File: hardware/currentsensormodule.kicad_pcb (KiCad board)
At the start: 2 copper layers, 92 x 54.5 mm, 110 parts, among them J101 USART, J102 STLink, J103 Sensor1, J104 Sensor2, J105 RJ45, J106 RJ45, U101 LM324, U103 K78L15-1000R3, U104 K78L15-1000R3, U105 AMS1117-5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

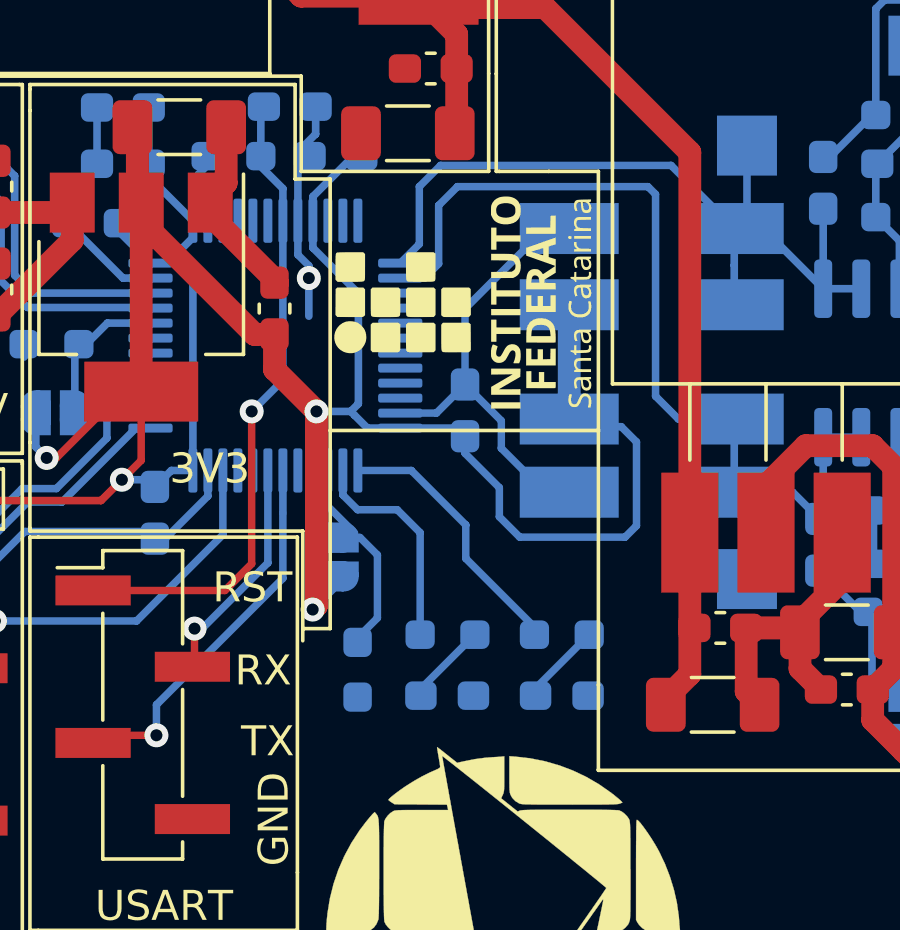
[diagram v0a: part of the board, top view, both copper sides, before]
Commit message: Pequenas mudanças na silkscreen
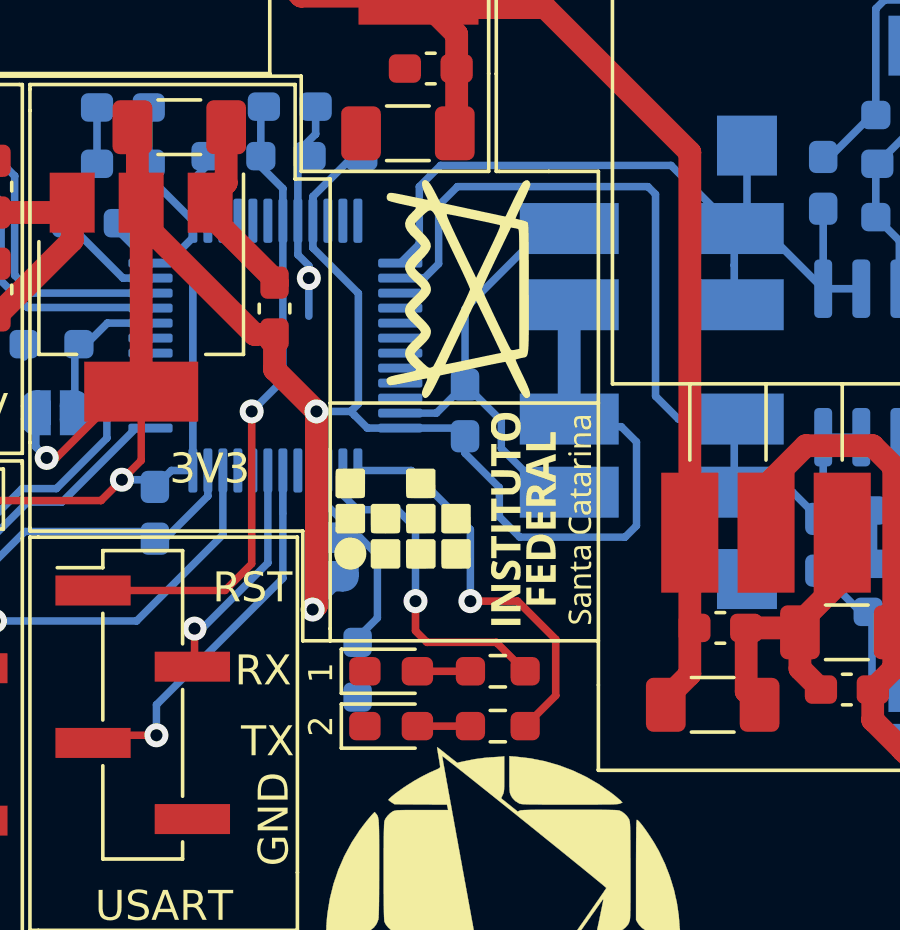
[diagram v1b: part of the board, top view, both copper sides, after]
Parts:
- added SYM105: SYM_Radioactive_Radiation_Small, naolavar:naolavar, F.Cu at (135.8, 98.1)
- D105, D106, R120, R121: moved to F.Cu
- moved SYM102 7.21 mm to (135.9, 105.8)
- moved D106 5.78 mm to (133.6, 112.7), turned to 0 degrees
- moved R120 3.72 mm to (137.1, 112.7), turned to 180 degrees
- moved R121 2.07 mm to (137.1, 110.9), turned to 180 degrees
- moved D105 2.04 mm to (133.6, 110.9), turned to 0 degrees
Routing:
- net /STM32/LED0: track 8.70 -> 13.6 mm, vias 0 -> 1
- net /STM32/LED1: track 7.31 -> 11.3 mm, vias 0 -> 1
- net Net-(D105-Pad2): track 2.78 -> 1.77 mm
- net Net-(D106-Pad2): track 2.77 -> 1.77 mm
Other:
- board text added: "1"
- board text added: "2"
- board text removed: "LED0"
- board text removed: "LED1"

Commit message: hardware: Design constraints adjusted according to JLC pcb limits
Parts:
- moved LOGO101 18.9 mm to (161.2, 76.8)
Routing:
- net +3V3: track 97.9 -> 97.2 mm
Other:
- board text added: "Designed by Zenite Solar Boat Team - github.com/ZeniteSolar"
- board text added: "github.com/ZeniteSolar/MSC22"

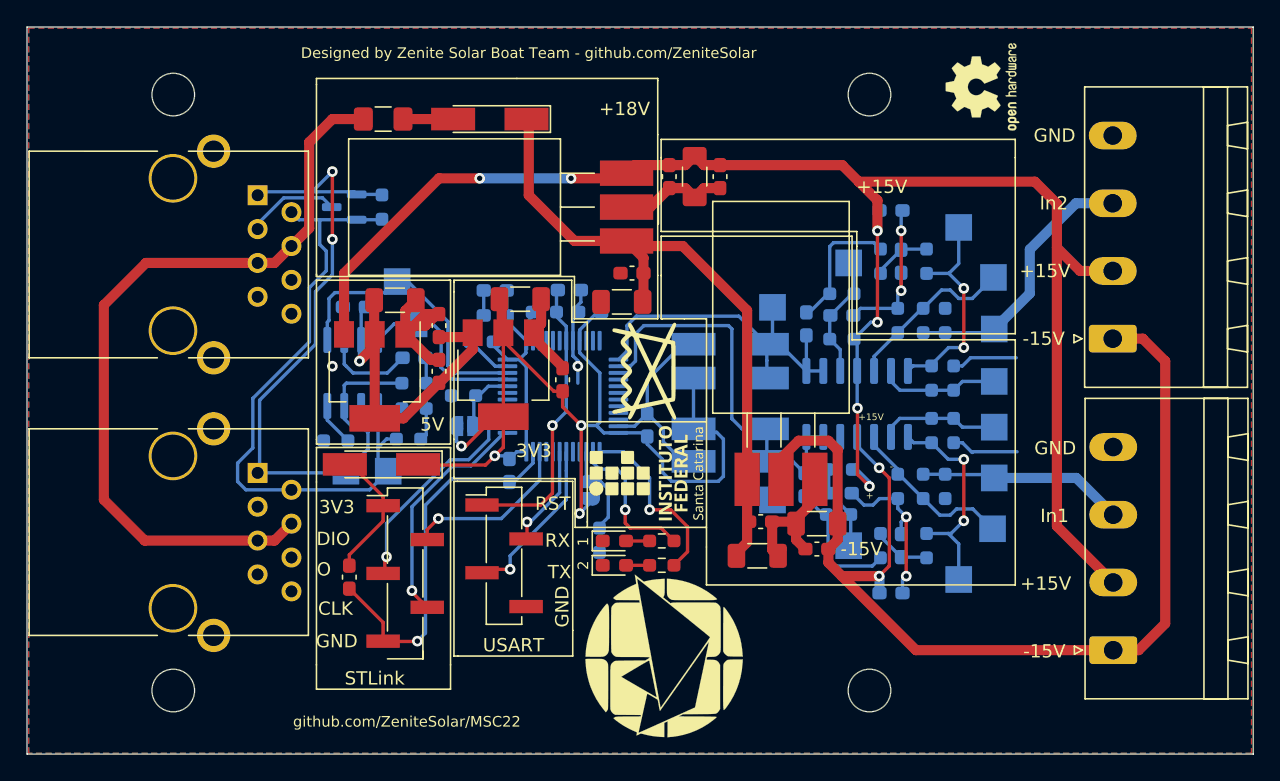
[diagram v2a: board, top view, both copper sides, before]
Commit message: hardware: Silkscreen ajusted, RDC errors fixed
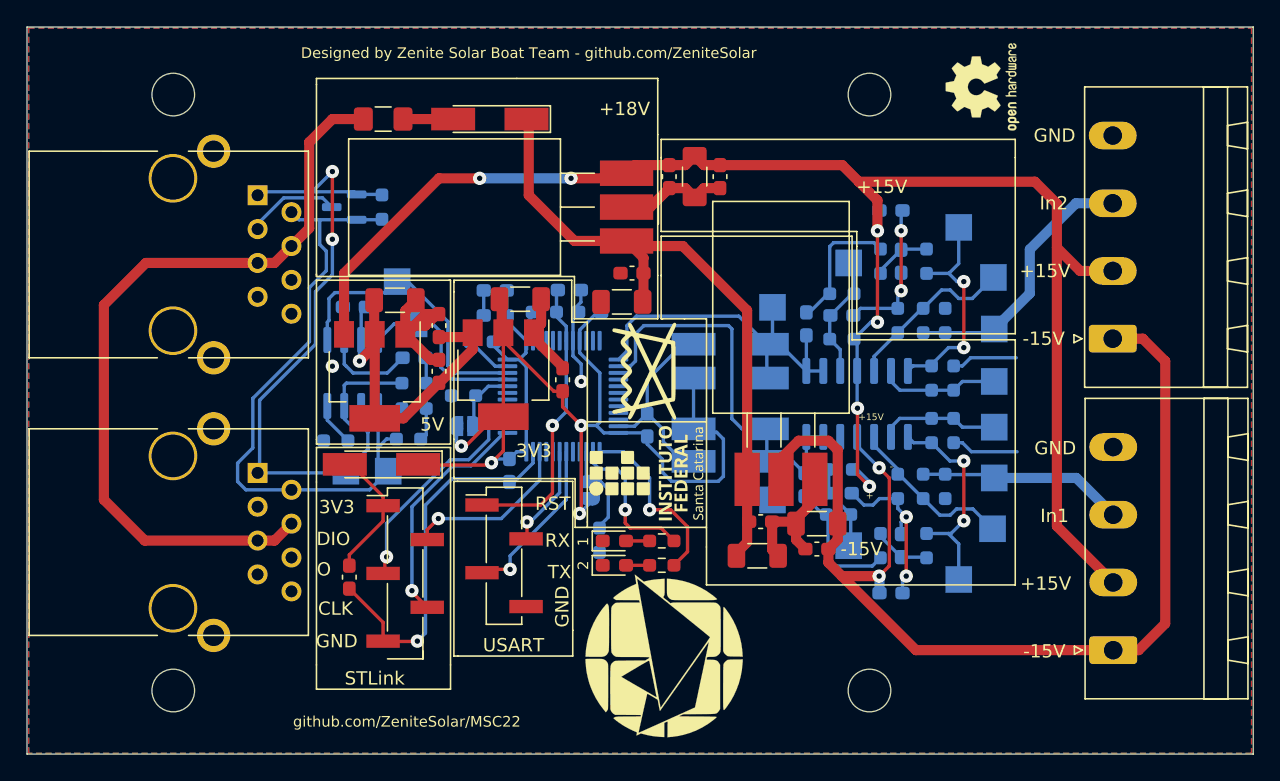
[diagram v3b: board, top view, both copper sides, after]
